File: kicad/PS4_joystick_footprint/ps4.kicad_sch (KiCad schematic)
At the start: 2 parts, among them J1 Joystick, U1 COM-09032

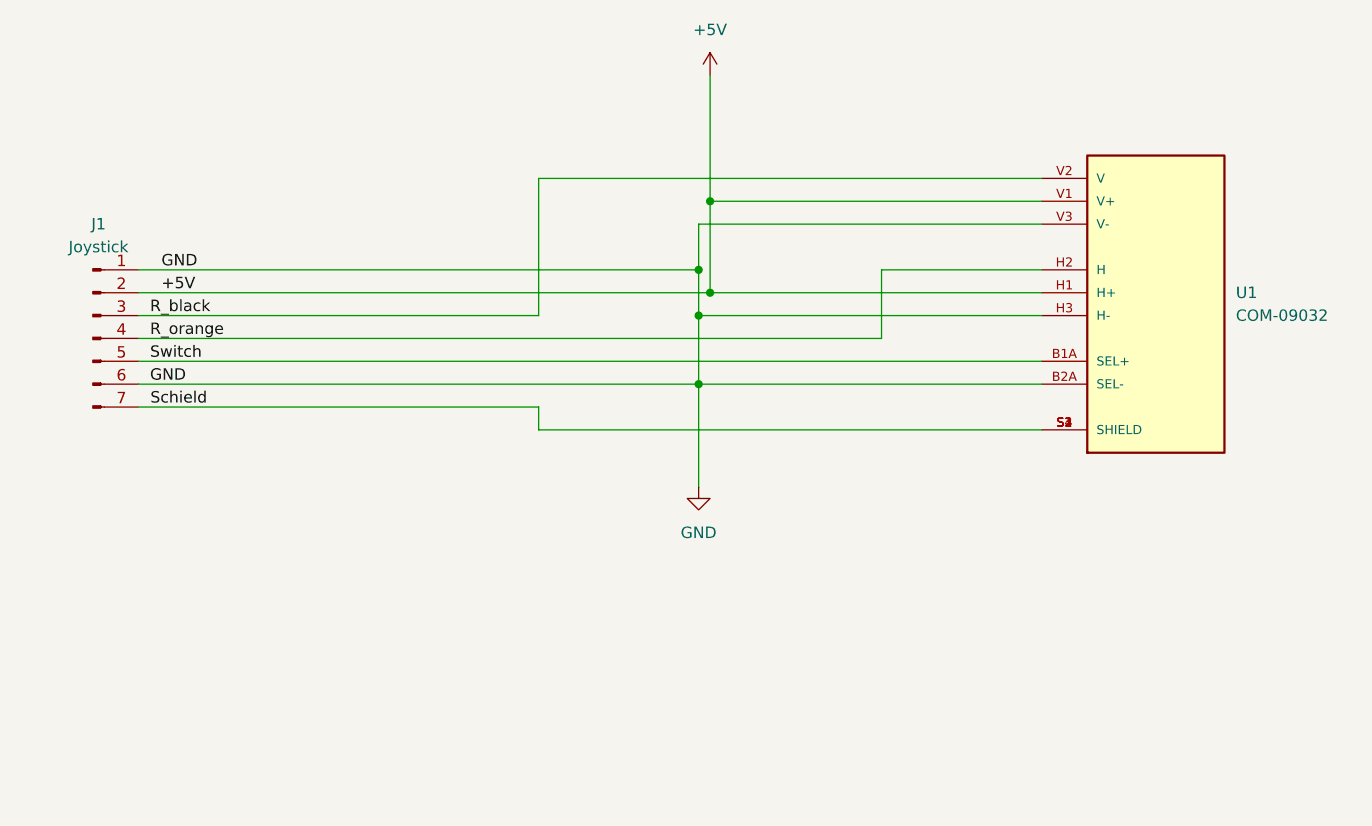
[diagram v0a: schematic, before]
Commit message: start to add button matrix to joystick pcb
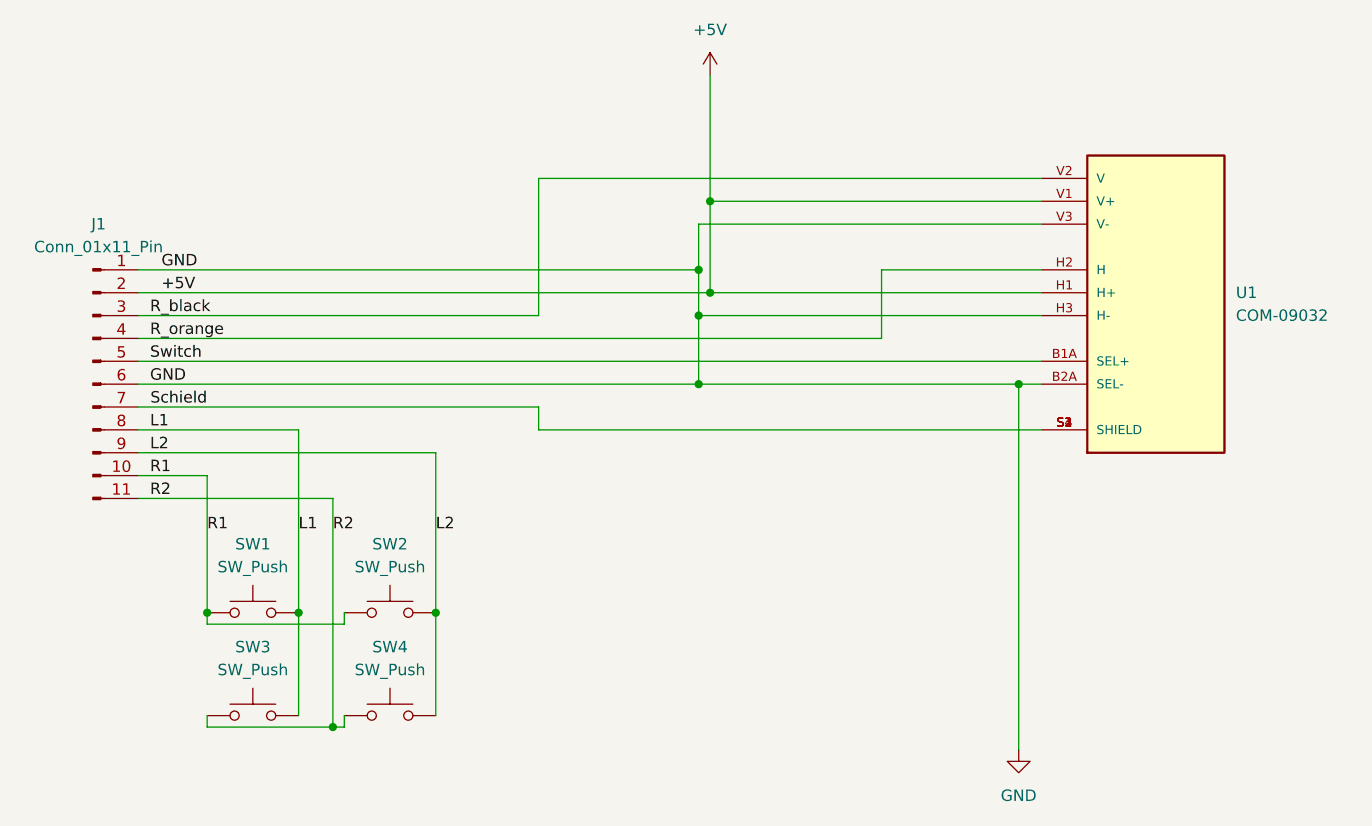
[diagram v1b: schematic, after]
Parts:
- removed J1: Joystick, Connector_PinHeader_2.54mm:PinHeader_1x07_P2.54mm_Vertical, symbol Connector:Conn_01x07_Pin
- added J1: Conn_01x11_Pin, Connector_PinHeader_2.54mm:PinHeader_1x11_P2.54mm_Vertical, symbol Connector:Conn_01x11_Pin
- added SW1, SW2, SW3, SW4: SW_Push, symbol Switch:SW_Push
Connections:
- net +5V: now also J1.2 (Pin_2)
- net GND: now also J1.1 (Pin_1), J1.6 (Pin_6)
- net R_black: now also J1.3 (Pin_3)
- net R_orange: now also J1.4 (Pin_4)
- net Schield: now also J1.7 (Pin_7)
- net Switch: now also J1.5 (Pin_5)
- new net L1: J1.8 (Pin_8), SW1.2, SW3.2
- new net L2: J1.9 (Pin_9), SW2.2, SW4.2
- new net R1: J1.10 (Pin_10), SW1.1, SW2.1
- new net R2: J1.11 (Pin_11), SW3.1, SW4.1

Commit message: update pcb and documentation
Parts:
- SW1, SW2, SW3, SW4: footprint (none) -> Button_Switch_SMD:SW_SPST_B3S-1000
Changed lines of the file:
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@@
 			)
 		)
-		(property "Footprint" ""
+		(property "Footprint" "Button_Switch_SMD:SW_SPST_B3S-1000"
 			(at 83.82 146.05 0)
 			(effects
@@
 			)
 		)
-		(property "Footprint" ""
+		(property "Footprint" "Button_Switch_SMD:SW_SPST_B3S-1000"
 			(at 83.82 134.62 0)
 			(effects
@@
 			)
 		)
-		(property "Footprint" ""
+		(property "Footprint" "Button_Switch_SMD:SW_SPST_B3S-1000"
 			(at 68.58 146.05 0)
 			(effects
@@
 			)
 		)
-		(property "Footprint" ""
+		(property "Footprint" "Button_Switch_SMD:SW_SPST_B3S-1000"
 			(at 68.58 134.62 0)
 			(effects

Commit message: update joystick pcb
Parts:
- SW1: value SW_Push -> X
- SW2: value SW_Push -> A
- SW3: value SW_Push -> B
- SW4: value SW_Push -> Y
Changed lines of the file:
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@@
 			)
 		)
-		(property "Value" "SW_Push"
+		(property "Value" "Y"
 			(at 83.82 146.05 0)
 			(effects
@@
 			)
 		)
-		(property "Value" "SW_Push"
+		(property "Value" "A"
 			(at 83.82 134.62 0)
 			(effects
@@
 			)
 		)
-		(property "Value" "SW_Push"
+		(property "Value" "B"
 			(at 68.58 146.05 0)
 			(effects
@@
 			)
 		)
-		(property "Value" "SW_Push"
+		(property "Value" "X"
 			(at 68.58 134.62 0)
 			(effects

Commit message: update release v1.0.0
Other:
- company: (none) -> https://github.com/lusmdl
- title: (none) -> PS4 Joystick with buttons PCB
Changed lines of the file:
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@@
 	(generator_version "8.0")
 	(paper "A4")
+	(title_block
+		(title "PS4 Joystick with buttons PCB")
+		(date "2025-01-14")
+		(rev "v1.0.0")
+		(company "https://github.com/lusmdl")
+	)
 	(junction
 		(at 119.38 104.14)

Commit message: optimize ps4 joystick pcb
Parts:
- added D1: D, Diode_SMD:D_MiniMELF, symbol Device:D
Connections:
- net +5V: now also D1.1 (K)
- net GND: now also D1.2 (A)
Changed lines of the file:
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@@
 	)
 	(junction
-		(at 118.11 101.6)
+		(at 118.11 96.52)
 		(diameter 0)
 		(color 0 0 0 0)
@@
 	)
 	(junction
+		(at 82.55 96.52)
+		(diameter 0)
+		(color 0 0 0 0)
+	)
+	(junction
 		(at 73.66 139.7)
 		(diameter 0)
 		(color 0 0 0 0)
 	)
+	(junction
+		(at 82.55 104.14)
+		(diameter 0)
+		(color 0 0 0 0)
+	)
 	(wire
 		(pts
@@
 	(wire
 		(pts
-			(xy 118.11 106.68) (xy 118.11 101.6)
+			(xy 82.55 104.14) (xy 119.38 104.14)
 		)
 		(stroke
@@
 	(wire
 		(pts
+			(xy 82.55 96.52) (xy 118.11 96.52)
+		)
+		(stroke
+			(width 0)
+			(type default)
+		)
+	)
+	(wire
+		(pts
 			(xy 55.88 124.46) (xy 63.5 124.46)
 		)
@@
 	(wire
 		(pts
+			(xy 67.31 101.6) (xy 67.31 96.52)
+		)
+		(stroke
+			(width 0)
+			(type default)
+		)
+	)
+	(wire
+		(pts
 			(xy 77.47 152.4) (xy 63.5 152.4)
 		)
@@
 	(wire
 		(pts
-			(xy 55.88 104.14) (xy 119.38 104.14)
+			(xy 55.88 104.14) (xy 82.55 104.14)
 		)
 		(stroke
@@
 	(wire
 		(pts
-			(xy 118.11 96.52) (xy 118.11 101.6)
-		)
-		(stroke
-			(width 0)
-			(type default)
-		)
-	)
-	(wire
-		(pts
 			(xy 156.21 96.52) (xy 118.11 96.52)
 		)
@@
 	(wire
 		(pts
-			(xy 55.88 101.6) (xy 118.11 101.6)
+			(xy 118.11 96.52) (xy 118.11 106.68)
 		)
 		(stroke
@@
 	(wire
 		(pts
+			(xy 55.88 101.6) (xy 67.31 101.6)
+		)
+		(stroke
+			(width 0)
+			(type default)
+		)
+	)
+	(wire
+		(pts
 			(xy 55.88 127) (xy 77.47 127)
 		)
@@
 		(pts
 			(xy 119.38 93.98) (xy 119.38 80.01)
+		)
+		(stroke
+			(width 0)
+			(type default)
+		)
+	)
+	(wire
+		(pts
+			(xy 67.31 96.52) (xy 82.55 96.52)
 		)
 		(stroke
@@
 	(label "L2"
 		(at 88.9 130.81 0)
-		(fields_autoplaced yes)
 		(effects
 			(font
@@
 	(label "GND"
 		(at 57.15 114.3 0)
-		(fields_autoplaced yes)
 		(effects
 			(font
@@
 	(label "L2"
 		(at 57.15 121.92 0)
-		(fields_autoplaced yes)
 		(effects
 			(font
@@
 	(label "R2"
 		(at 57.15 127 0)
-		(fields_autoplaced yes)
 		(effects
 			(font
@@
 	(label "GND"
 		(at 58.42 101.6 0)
-		(fields_autoplaced yes)
 		(effects
 			(font
@@
 	(label "R1"
 		(at 57.15 124.46 0)
-		(fields_autoplaced yes)
 		(effects
 			(font
@@
 	(label "L1"
 		(at 57.15 119.38 0)
-		(fields_autoplaced yes)
 		(effects
 			(font
@@
 	(label "R_orange"
 		(at 57.15 109.22 0)
-		(fields_autoplaced yes)
 		(effects
 			(font
@@
 	(label "R2"
 		(at 77.47 130.81 0)
-		(fields_autoplaced yes)
 		(effects
 			(font
@@
 	(label "Switch"
 		(at 57.15 111.76 0)
-		(fields_autoplaced yes)
 		(effects
 			(font
@@
 	(label "Schield"
 		(at 63.5 116.84 180)
-		(fields_autoplaced yes)
 		(effects
 			(font
@@
 	(label "R_black"
 		(at 57.15 106.68 0)
-		(fields_autoplaced yes)
 		(effects
 			(font
@@
 	(label "L1"
 		(at 73.66 130.81 0)
-		(fields_autoplaced yes)
 		(effects
 			(font
@@
 	(label "R1"
 		(at 63.5 130.81 0)
-		(fields_autoplaced yes)
 		(effects
 			(font
@@
 	(label "+5V"
 		(at 58.42 104.14 0)
-		(fields_autoplaced yes)
 		(effects
 			(font
@@
 					(unit 1)
 				)
+			)
+		)
+	)
+	(symbol
+		(lib_id "Device:D")
+		(at 82.55 100.33 90)
+		(unit 1)
+		(exclude_from_sim no)
+		(in_bom yes)
+		(on_board yes)
+		(dnp no)
+		(fields_autoplaced yes)
+		(property "Reference" "D1"
+			(at 85.09 99.0599 90)
+			(effects
+				(font
+					(size 1.27 1.27)
+				)
+				(justify right)
+			)
+		)
+		(property "Value" "D"
+			(at 85.09 101.5999 90)
+			(effects
+				(font
+					(size 1.27 1.27)
+				)
+				(justify right)
+			)
+		)
+		(property "Footprint" "Diode_SMD:D_MiniMELF"
+			(at 82.55 100.33 0)
+			(effects
+				(font
+					(size 1.27 1.27)
+				)
+				(hide yes)
+			)
+		)
+		(property "Datasheet" "~"
+			(at 82.55 100.33 0)
+			(effects
+				(font
+					(size 1.27 1.27)
+				)
+				(hide yes)
+			)
+		)
+		(property "Description" "Diode"
+			(at 82.55 100.33 0)
+			(effects
+				(font
+					(size 1.27 1.27)
+				)
+				(hide yes)
+			)
+		)
+		(property "Sim.Device" "D"
+			(at 82.55 100.33 0)
+			(effects
+				(font
+					(size 1.27 1.27)
+				)
+				(hide yes)
+			)
+		)
+		(property "Sim.Pins" "1=K 2=A"
+			(at 82.55 100.33 0)
+			(effects
+				(font
+					(size 1.27 1.27)
+				)
+				(hide yes)
+			)
+		)
+		(pin "1"
+		)
+		(pin "2"
+		)
+		(instances
+			(project ""
+				(path "/5aa25748-904e-4465-bad4-f422c48ad736"
+					(reference "D1")
+					(unit 1)
+				)
